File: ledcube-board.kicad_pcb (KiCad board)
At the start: 4 copper layers, 100.8 x 86.8 mm, 181 parts, among them J1 Conn_01x02, J10 molex_53261-0871, J11 104031-0811, J12 molex_53261-0871, J2 molex_53261-0871, J3 molex_53261-0871, J4 molex_53261-0871, J5 molex_53261-0871, J6 molex_53261-0871, J7 molex_53261-0871, J8 molex_53261-0871, J9 molex_53261-0871, Q1 Q_NMOS_GDSD, Q2 Q_NMOS_GDSD, Q3 Q_NMOS_GDSD, Q4 Q_NMOS_GDSD, Q5 Q_NMOS_GDSD, Q6 Q_NMOS_GDSD, Q7 Q_NMOS_GDSD, Q8 Q_NMOS_GDSD, U1 LM1085IS-12, U10 ESP32-DEVKITC-32D, U11 IP4220CZ6, U12 IP4220CZ6, U13 XC9572XL-VQ64, U14 SN74LVCC3245APWR, U15 SN74LVCC3245APWR, U2 STP08CP05MTR, U3 STP08CP05MTR, U4 STP08CP05MTR, U5 STP08CP05MTR, U6 STP08CP05MTR, U7 STP08CP05MTR, U8 STP08CP05MTR, U9 STP08CP05MTR, X1 ASE-40MHz, X2 ASE-25MHz

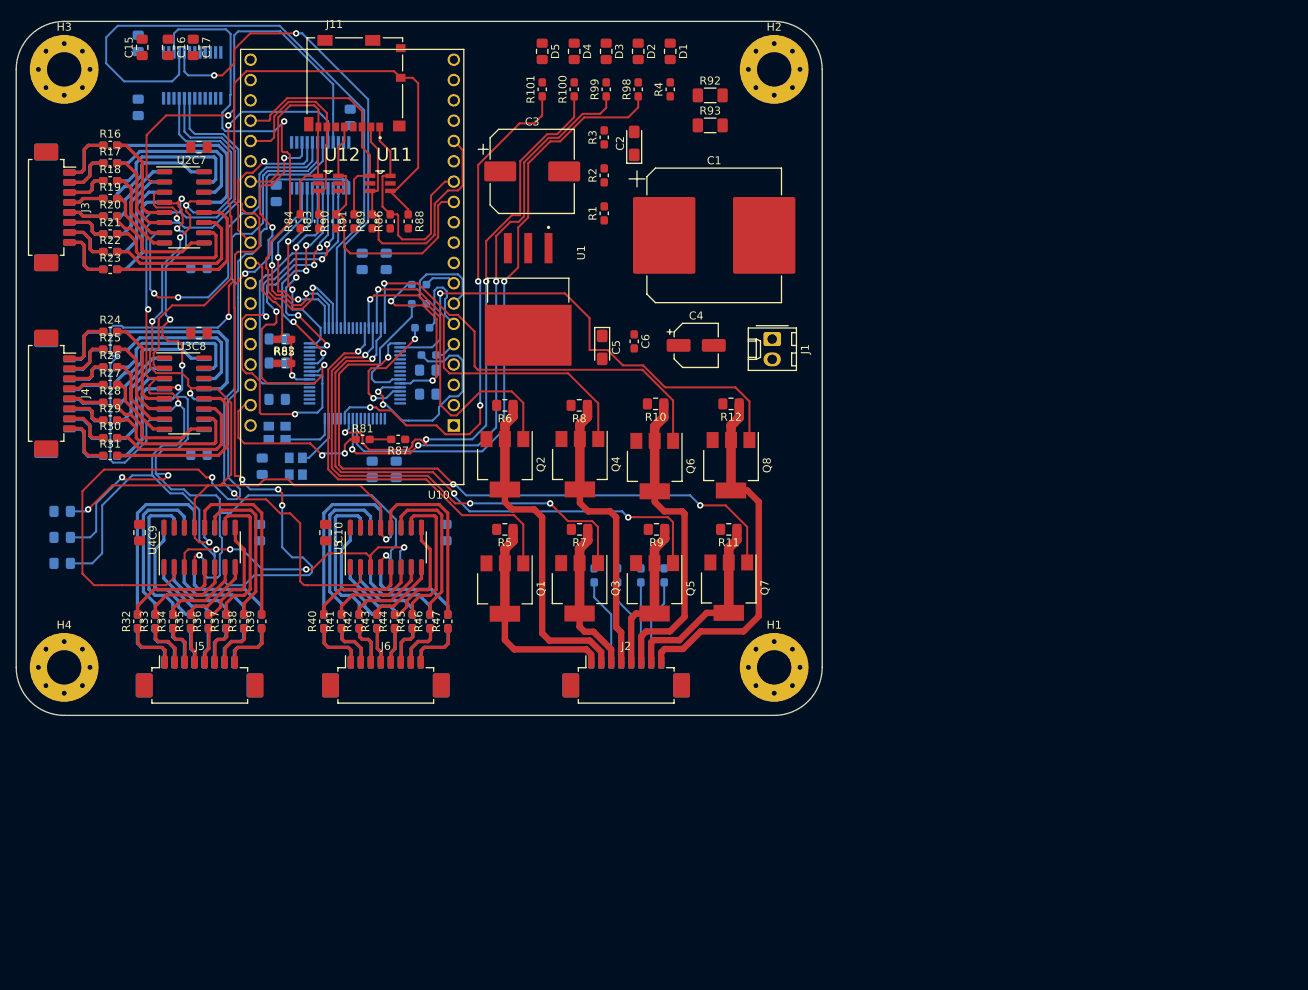
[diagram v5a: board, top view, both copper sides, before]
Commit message: PCB: complete placement
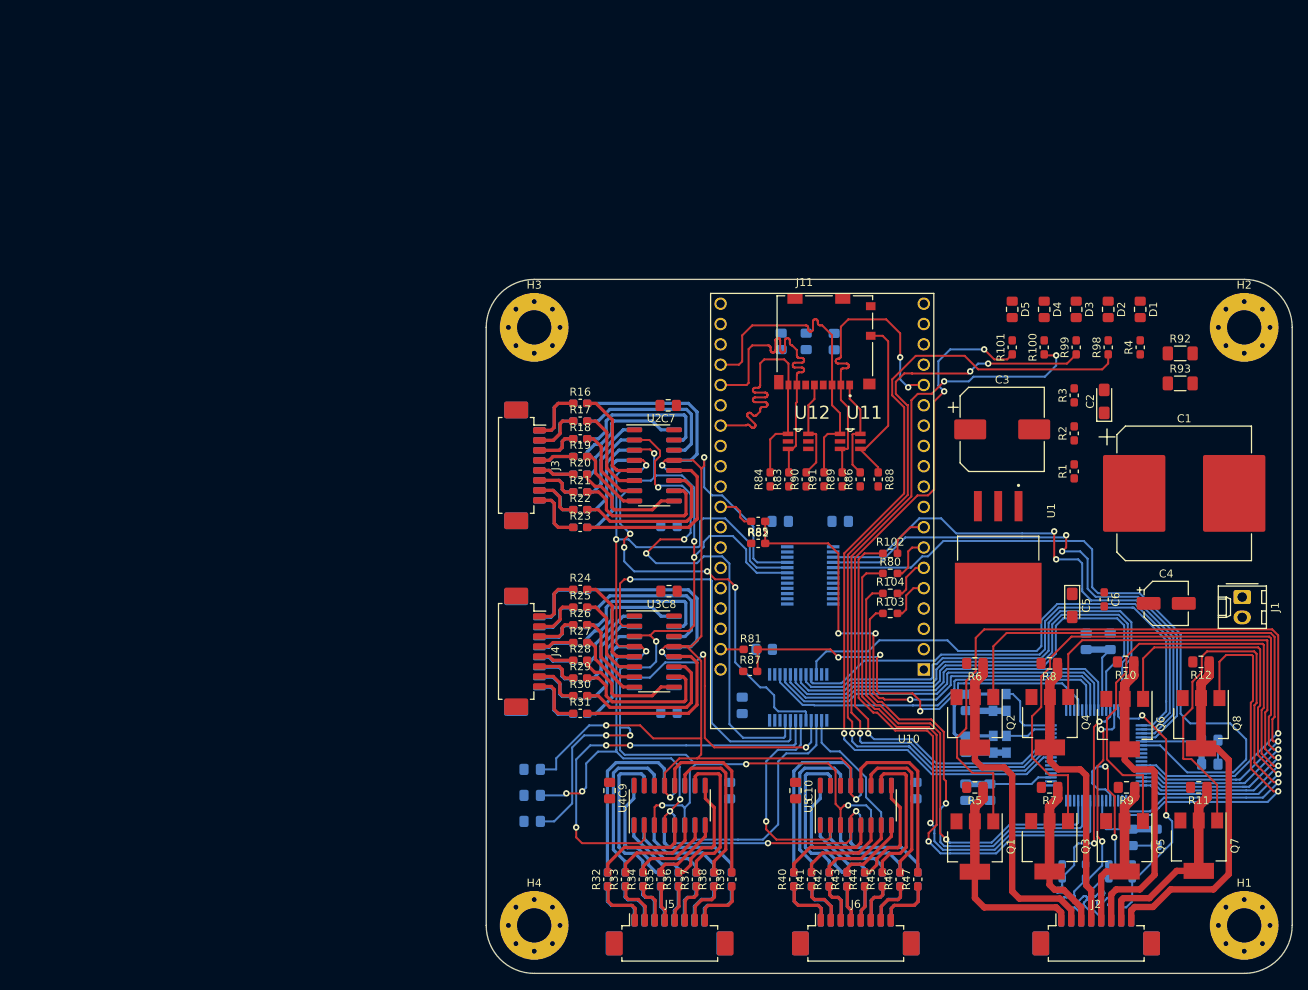
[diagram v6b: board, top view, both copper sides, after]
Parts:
- C15, C16, C17: moved to B.Cu
- R102, R103, R104, R80: moved to F.Cu
- moved C25 122.6 mm to (181.2, 117.5), turned to 270 degrees
- moved C30 117.8 mm to (178.2, 117.5), turned to 270 degrees
- moved C20 108.1 mm to (187.9, 108.3)
- moved C28 108.1 mm to (187.9, 105.3)
- moved U13 104.3 mm to (173.8, 107.2), turned to 0 degrees
- moved C26 104.0 mm to (160.4, 111.8), turned to 270 degrees
- moved C31 103.0 mm to (157.4, 111.8), turned to 270 degrees
- moved C24 101.9 mm to (141.8, 78.0), turned to 180 degrees
- moved C23 100.1 mm to (134.2, 78.0), turned to 180 degrees
- moved U15 99.4 mm to (138.0, 84.8), turned to 180 degrees
- moved X2 96.4 mm to (161.7, 100.6), turned to 90 degrees
- moved C29 94.7 mm to (175.5, 93.0), turned to 90 degrees
- moved C18 94.6 mm to (157.5, 105.9)
- moved X1 94.6 mm to (161.7, 105.9)
- moved C19 94.1 mm to (157.5, 100.6), turned to 90 degrees
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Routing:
- net /pl.sch/I2C_SDA: track 6.92 -> 67.5 mm, vias 1 -> 3
- net /DATA_LED4: track 80.6 -> 26.9 mm
- net /pl.sch/GPIO0: track 15.3 -> 68.5 mm, vias 0 -> 1
- net /DATA_LED7: track 82.0 -> 29.9 mm, vias 6 -> 0
- net /pl.sch/I2C_SCL: track 2.69 -> 54.4 mm, vias 0 -> 3
- net /DATA_LED3: track 100.5 -> 51.7 mm, vias 1 -> 3
- net /pl.sch/GPIO1: track 22.2 -> 69.5 mm, vias 2 -> 1
- net /LAYER_SEL1: track 52.5 -> 97.9 mm
- net /pl.sch/GPIO3: track 16.2 -> 59.6 mm, vias 2 -> 1
- net /ps.sch/SD_CD: track 64.1 -> 21.6 mm
- net /pl.sch/DATA_ROW7_3V3: track 24.1 -> 65.8 mm, vias 2 -> 0
- net /pl.sch/VCC_3V3: track 11.8 -> 52.7 mm
- net /pl.sch/DATA_ROW8_3V3: track 26.7 -> 67.3 mm, vias 2 -> 0
- net /DATA_LED6: track 77.3 -> 37.1 mm
- net /pl.sch/DATA_ROW6_3V3: track 24.4 -> 60.6 mm, vias 2 -> 0
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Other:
- net class pwr_3v3 added: clearance 0.2, trace_width 0.8, via_dia 1.2, via_drill 0.8

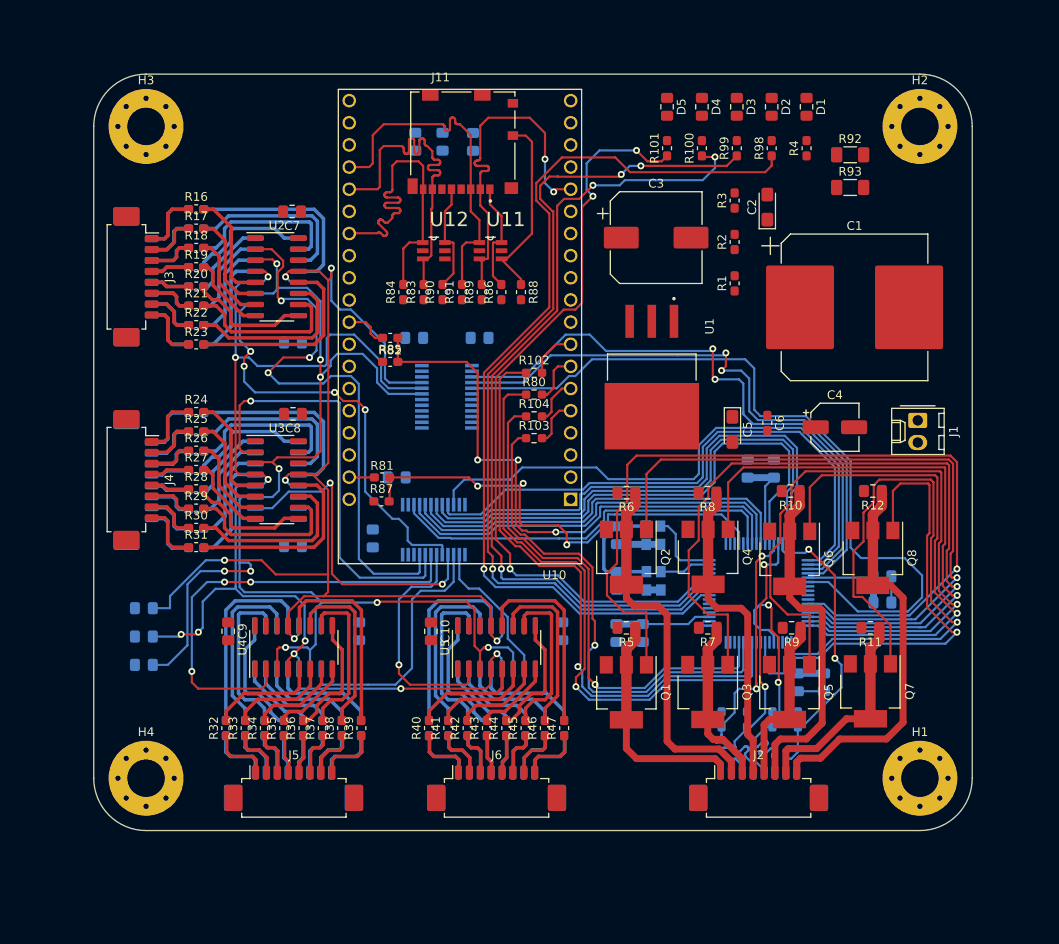
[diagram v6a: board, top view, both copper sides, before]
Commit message: Complete PCB placement and routing
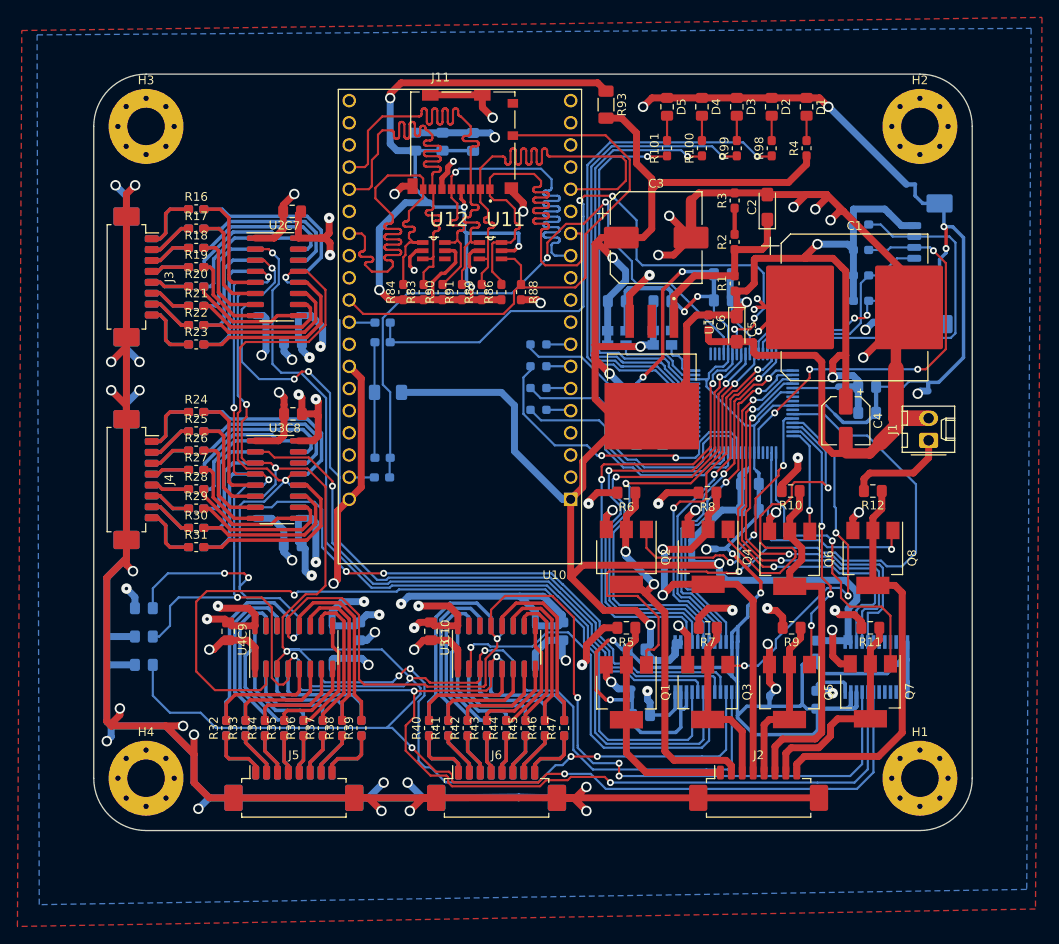
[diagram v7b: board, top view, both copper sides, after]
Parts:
- added NT1: Net-Tie_2, NetTie:NetTie-2_SMD_Pad0.5mm, B.Cu at (159.2, 118.8)
- added NT2: Net-Tie_2, NetTie:NetTie-2_SMD_Pad0.5mm, B.Cu at (175.0, 119.8)
- added NT3: Net-Tie_2, NetTie:NetTie-2_SMD_Pad0.5mm, B.Cu at (193.2, 83.6)
- added NT4: Net-Tie_2, NetTie:NetTie-2_SMD_Pad0.5mm, B.Cu at (189.0, 76.2)
- added NT5: Net-Tie_2, NetTie:NetTie-2_SMD_Pad0.5mm, B.Cu at (191.2, 60.4)
- added NT6: Net-Tie_2, NetTie:NetTie-2_SMD_Pad0.5mm, B.Cu at (169.4, 102.2)
- R102, R103, R104, R80, R81, R82, R85, R87, R92: moved to B.Cu
- moved J12 64.0 mm to (194.0, 69.5), turned to 270 degrees
- moved R92 59.6 mm to (131.2, 84.2)
- moved C23 58.5 mm to (180.5, 113.8), turned to 90 degrees
- moved U15 58.2 mm to (187.2, 115.8), turned to 270 degrees
- moved R97 57.2 mm to (185.5, 65.0), turned to 0 degrees
- moved C24 56.8 mm to (180.5, 119.5), turned to 90 degrees
- moved R96 54.8 mm to (185.5, 67.9), turned to 0 degrees
- moved R95 52.6 mm to (185.5, 70.8), turned to 0 degrees
- moved R94 50.6 mm to (185.5, 73.8), turned to 0 degrees
- moved C31 42.9 mm to (169.7, 70.7), turned to 180 degrees
- moved C26 39.2 mm to (169.7, 73.7), turned to 180 degrees
- moved C22 36.8 mm to (160.3, 121.2), turned to 0 degrees
- moved U14 35.0 mm to (167.8, 115.8)
- moved C21 33.9 mm to (159.8, 113.8)
- moved C18 32.1 mm to (157.5, 73.8), turned to 0 degrees
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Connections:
- C18 pad 2: GND -> GNDD
- C19 pad 2: GND -> GNDD
- C20 pad 2: GND -> GNDD
- C21 pad 1: GND -> GNDD
- C22 pad 1: GND -> GNDD
- C23 pad 1: GND -> GNDD
- C24 pad 1: GND -> GNDD
- C25 pad 2: GND -> GNDD
- C26 pad 2: GND -> GNDD
- C27 pad 2: GND -> GNDD
- C28 pad 2: GND -> GNDD
- C29 pad 2: GND -> GNDD
- C30 pad 2: GND -> GNDD
- C31 pad 2: GND -> GNDD
- J12 pad 7: GND -> GNDD
- J12 pad 8: GND -> GNDD
- J12 pad MP: GND -> GNDD
- U13 pad 14: GND -> GNDD
- U13 pad 21: GND -> GNDD
- U13 pad 41: GND -> GNDD
- U13 pad 54: GND -> GNDD
- U14 pad 11: GND -> GNDD
- U14 pad 12: GND -> GNDD
- U14 pad 13: GND -> GNDD
- U14 pad 22: GND -> GNDD
- U14 pad 23: GND -> GNDD
- U15 pad 11: GND -> GNDD
- U15 pad 12: GND -> GNDD
- U15 pad 13: GND -> GNDD
- U15 pad 22: GND -> GNDD
- U15 pad 23: GND -> GNDD
- X1 pad 2: GND -> GNDD
- X2 pad 2: GND -> GNDD
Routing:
- net GND: track 26.0 -> 650.6 mm, vias 0 -> 57
- net /pl.sch/VCC_3V3: track 52.7 -> 371.2 mm, vias 0 -> 8
- net GNDD: track 0.00 -> 298.2 mm, vias 0 -> 10
- net /pl.sch/VCC_5V0: track 0.00 -> 197.1 mm, vias 0 -> 29
- net SD_3V3: track 0.00 -> 111.5 mm, vias 0 -> 5
- net /layer_led_mux.sch/CLK: track 151.5 -> 228.0 mm, vias 9 -> 8
- net /pl.sch/~DATA_OE_5V5: track 134.9 -> 204.6 mm, vias 6 -> 9
- net /DATA_LED5: track 49.0 -> 109.0 mm, vias 4 -> 2
- net /LAYER_SEL5: track 78.1 -> 30.1 mm, vias 1 -> 3
- net /pl.sch/LED_R: track 107.6 -> 60.0 mm
- net /pl.sch/LED_O1: track 95.0 -> 48.7 mm, vias 3 -> 1
- net /pl.sch/LED_G: track 100.4 -> 54.3 mm, vias 3 -> 1
- net /pl.sch/LED_O2: track 88.8 -> 42.9 mm, vias 3 -> 1
- net /LAYER_SEL3: track 87.5 -> 41.6 mm, vias 1 -> 3
- net /DATA_LED3: track 51.7 -> 97.4 mm, vias 3 -> 1
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- added copper zone on B.Cu, net (none)
- added copper zone on F.Cu, net (none)
- added copper zone on In2.Cu, net /pl.sch/VCC_5V0
- added copper zone on In1.Cu, net GND
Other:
- net class digit_gnd added: clearance 0.2, trace_width 0.4, via_dia 0.8, via_drill 0.4
- net class pwr_5v0 added: clearance 0.2, trace_width 0.8, via_dia 1.2, via_drill 0.4
- net class pwr_gnd added: clearance 0.2, trace_width 0.8, via_dia 1.2, via_drill 0.8
- net class pwr_sd added: clearance 0.2, trace_width 0.8, via_dia 1.2, via_drill 0.8

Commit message: Update PCB traces
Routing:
- net /pl.sch/TCK: track 44.5 -> 30.2 mm
- net /pl.sch/TDI: track 23.1 -> 29.8 mm
- net /pl.sch/TMS: track 25.3 -> 30.3 mm, vias 0 -> 4
- net GNDD: track 298.2 -> 293.4 mm
- net /ps.sch/SD_DAT2: track 54.7 -> 57.0 mm
- net /ps.sch/SD_DAT3: track 55.6 -> 57.3 mm, vias 0 -> 2
- net /ps.sch/SD_DAT0: track 56.7 -> 58.0 mm, vias 0 -> 2
- net GND: track 650.6 -> 651.6 mm
- net /ps.sch/SD_CLK: track 56.7 -> 57.5 mm, vias 1 -> 2
- net /ps.sch/SD_DAT1: track 56.6 -> 57.5 mm
- net /pl.sch/VCC_3V3: track 371.2 -> 372.0 mm
- net /ps.sch/SD_CMD: track 56.6 -> 57.1 mm, vias 0 -> 2
